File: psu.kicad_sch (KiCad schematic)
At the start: 21 parts, among them J17 Barrel_Jack_Switch, J18 USB_C_Receptacle_USB2.0_16P

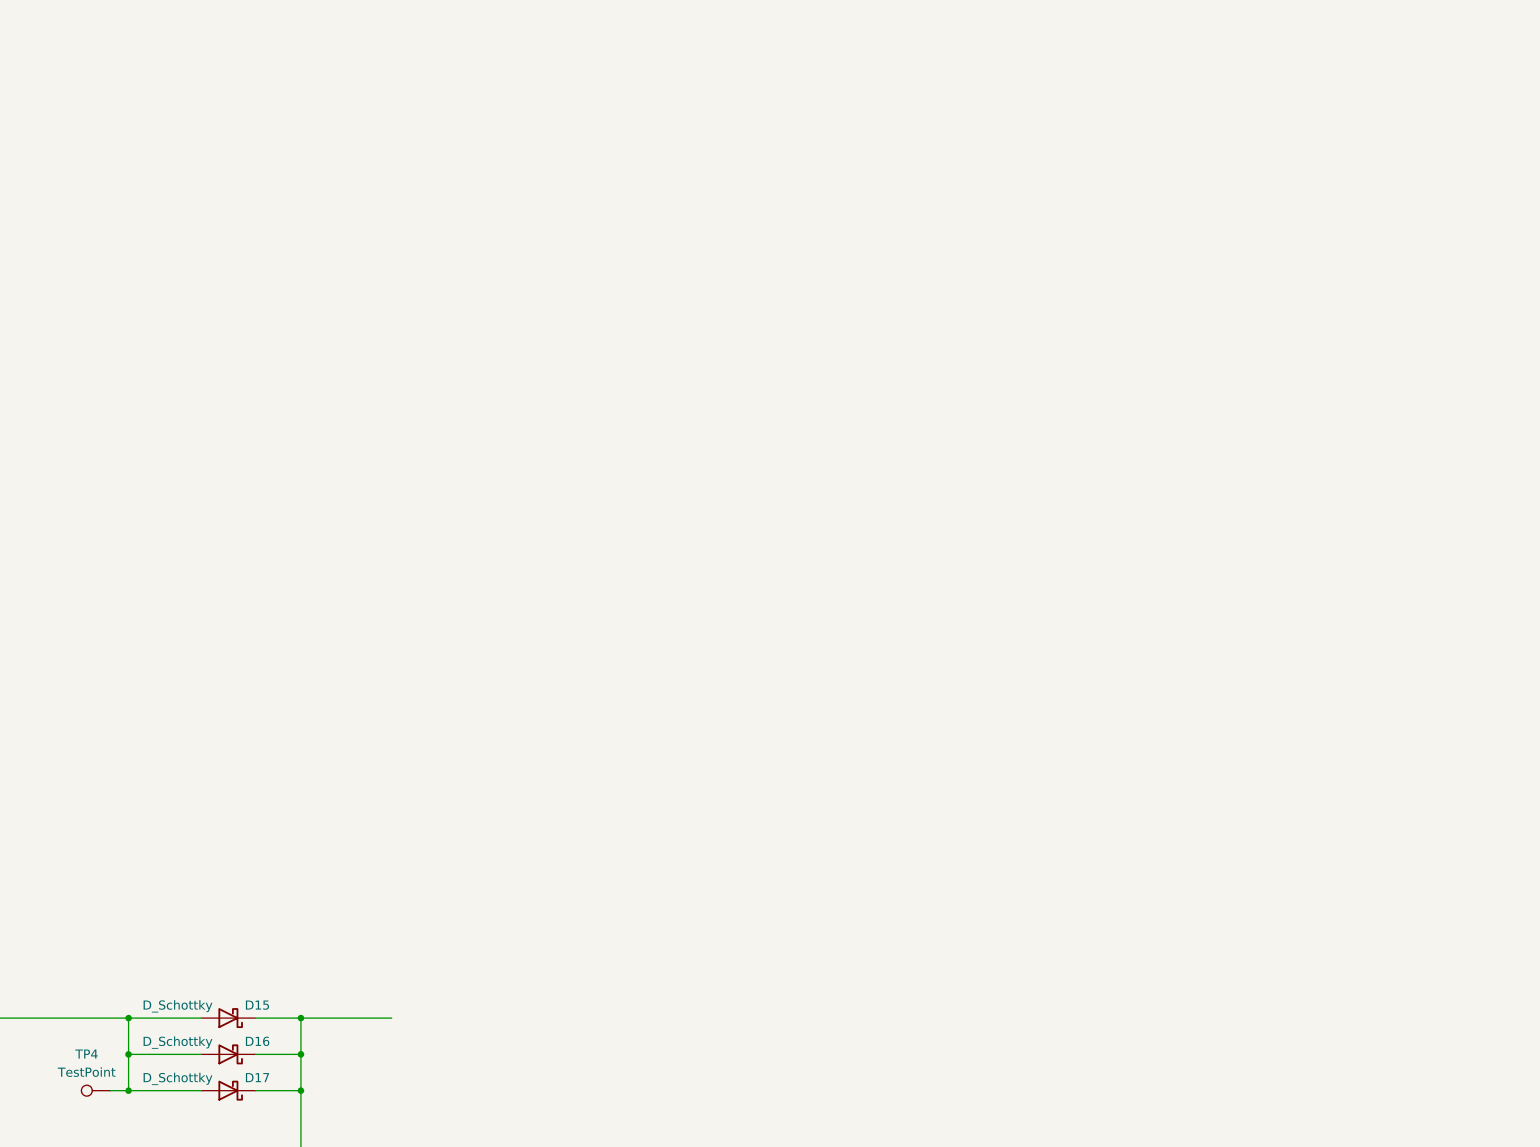
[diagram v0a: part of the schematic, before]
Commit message: feat(psu): Added PCIe power
- Do not populate, but there for future possible use.
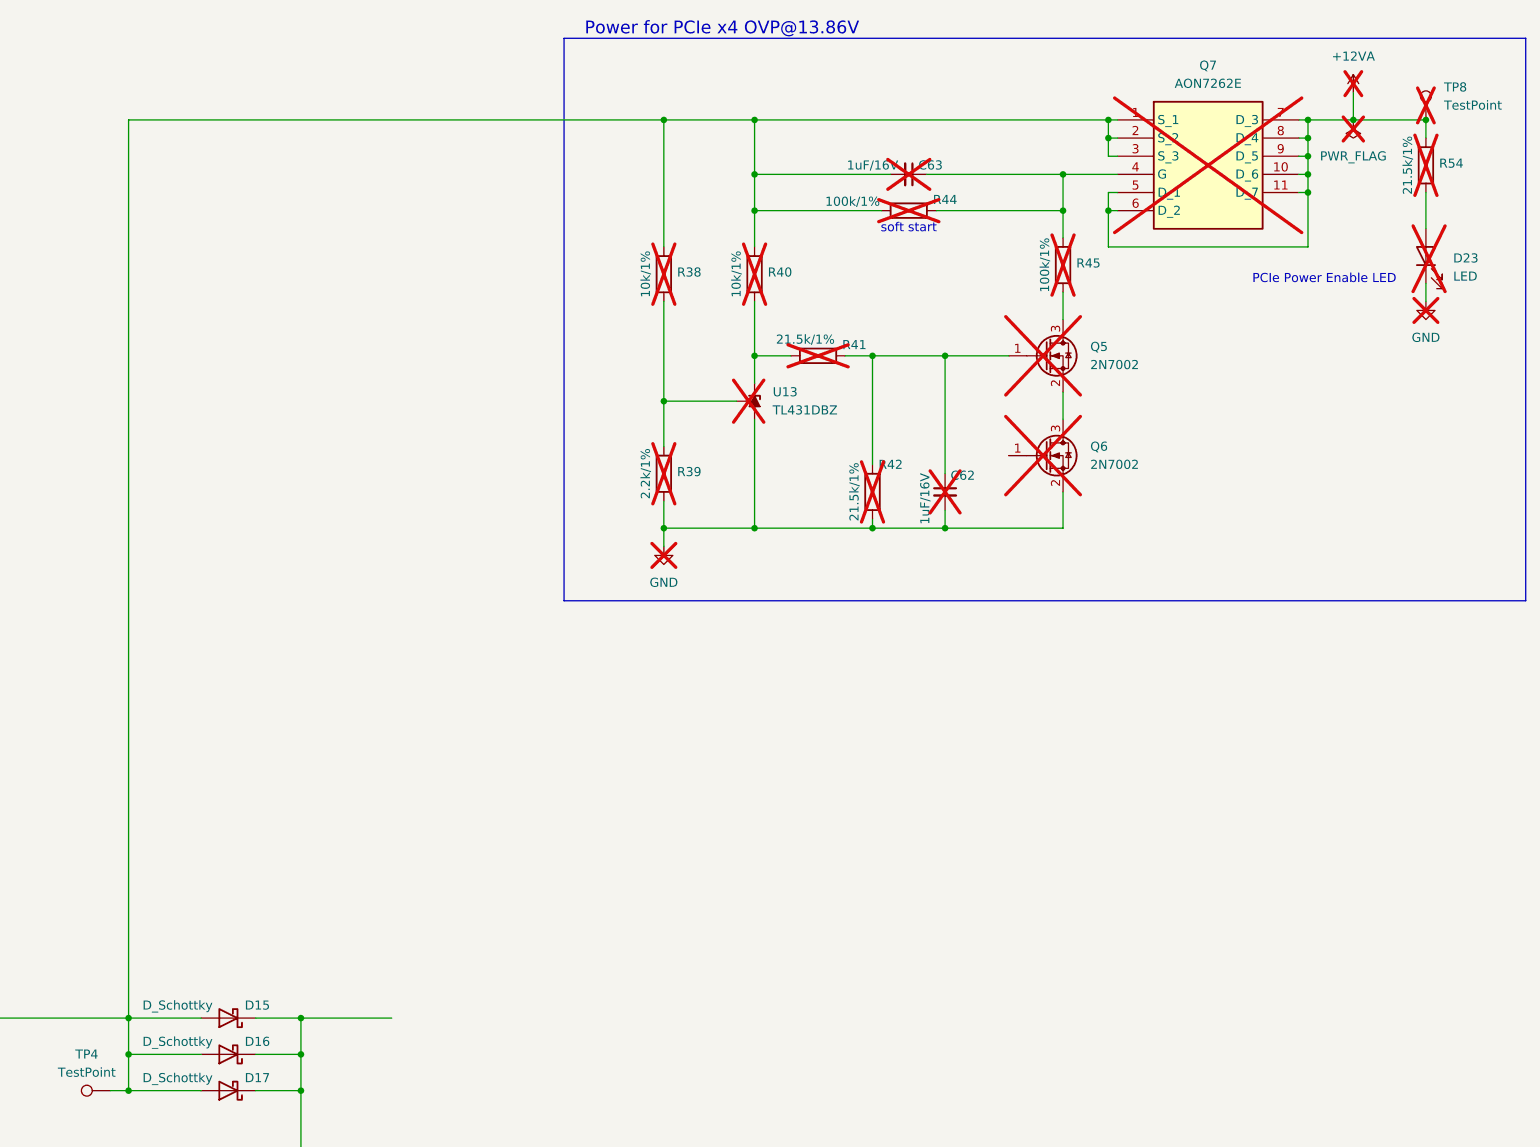
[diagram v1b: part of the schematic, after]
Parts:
- added C62, C63: 1uF/16V, A_HDJ_Library:C_0402_1005Metric, symbol Device:C_Small
- added D23: LED, A_HDJ_Library:LED_0603_1608Metric, symbol Device:LED
- added Q5, Q6: 2N7002, A_HDJ_Library:SOT-23, symbol Transistor_FET:2N7002
- added Q7: AON7262E, A_HDJ_Library:MOSFET_PDFN8_3.3x3.3, symbol A_HDJ_Library:AON7262E
- added R38, R40: 10k/1%, A_HDJ_Library:R_0402_1005Metric, symbol Device:R
- added R39: 2.2k/1%, A_HDJ_Library:R_0402_1005Metric, symbol Device:R
- added R41, R42, R54: 21.5k/1%, A_HDJ_Library:R_0402_1005Metric, symbol Device:R
- added R44, R45: 100k/1%, A_HDJ_Library:R_0402_1005Metric, symbol Device:R
- added TP8: TestPoint, symbol Connector:TestPoint
- added U13: TL431DBZ, A_HDJ_Library:SOT-23, symbol Reference_Voltage:TL431DBZ
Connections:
- net GND: now also C62.2, D23.1 (K), Q6.2 (S), R39.1, R42.1, U13.3 (A)
- net at D15.2 (A), D16.2 (A), D17.2 (A)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: now also C63.2, Q7.1 (S_1), Q7.2 (S_2), Q7.3 (S_3), R38.2, R40.2, R44.1
- new net: R38.1, R39.2, U13.2 (REF)
- new net: R40.1, R41.1, U13.1 (K)
- new net: C62.1, Q5.1 (G), R41.2, R42.2
- new net: Q5.2 (S), Q6.3 (D)
- new net: D23.2 (A), R54.1
- new net: C63.1, Q7.4 (G), R44.2, R45.2
- new net: Q5.3 (D), R45.1
- new net +12VA: Q7.10 (D_6), Q7.11 (D_7), Q7.5 (D_1), Q7.6 (D_2), Q7.7 (D_3), Q7.8 (D_4), Q7.9 (D_5), R54.2, TP8.1
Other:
- note added: "PCIe Power Enable LED"
- note added: "Power for PCIe x4 OVP@13.86V"
- note added: "soft start"

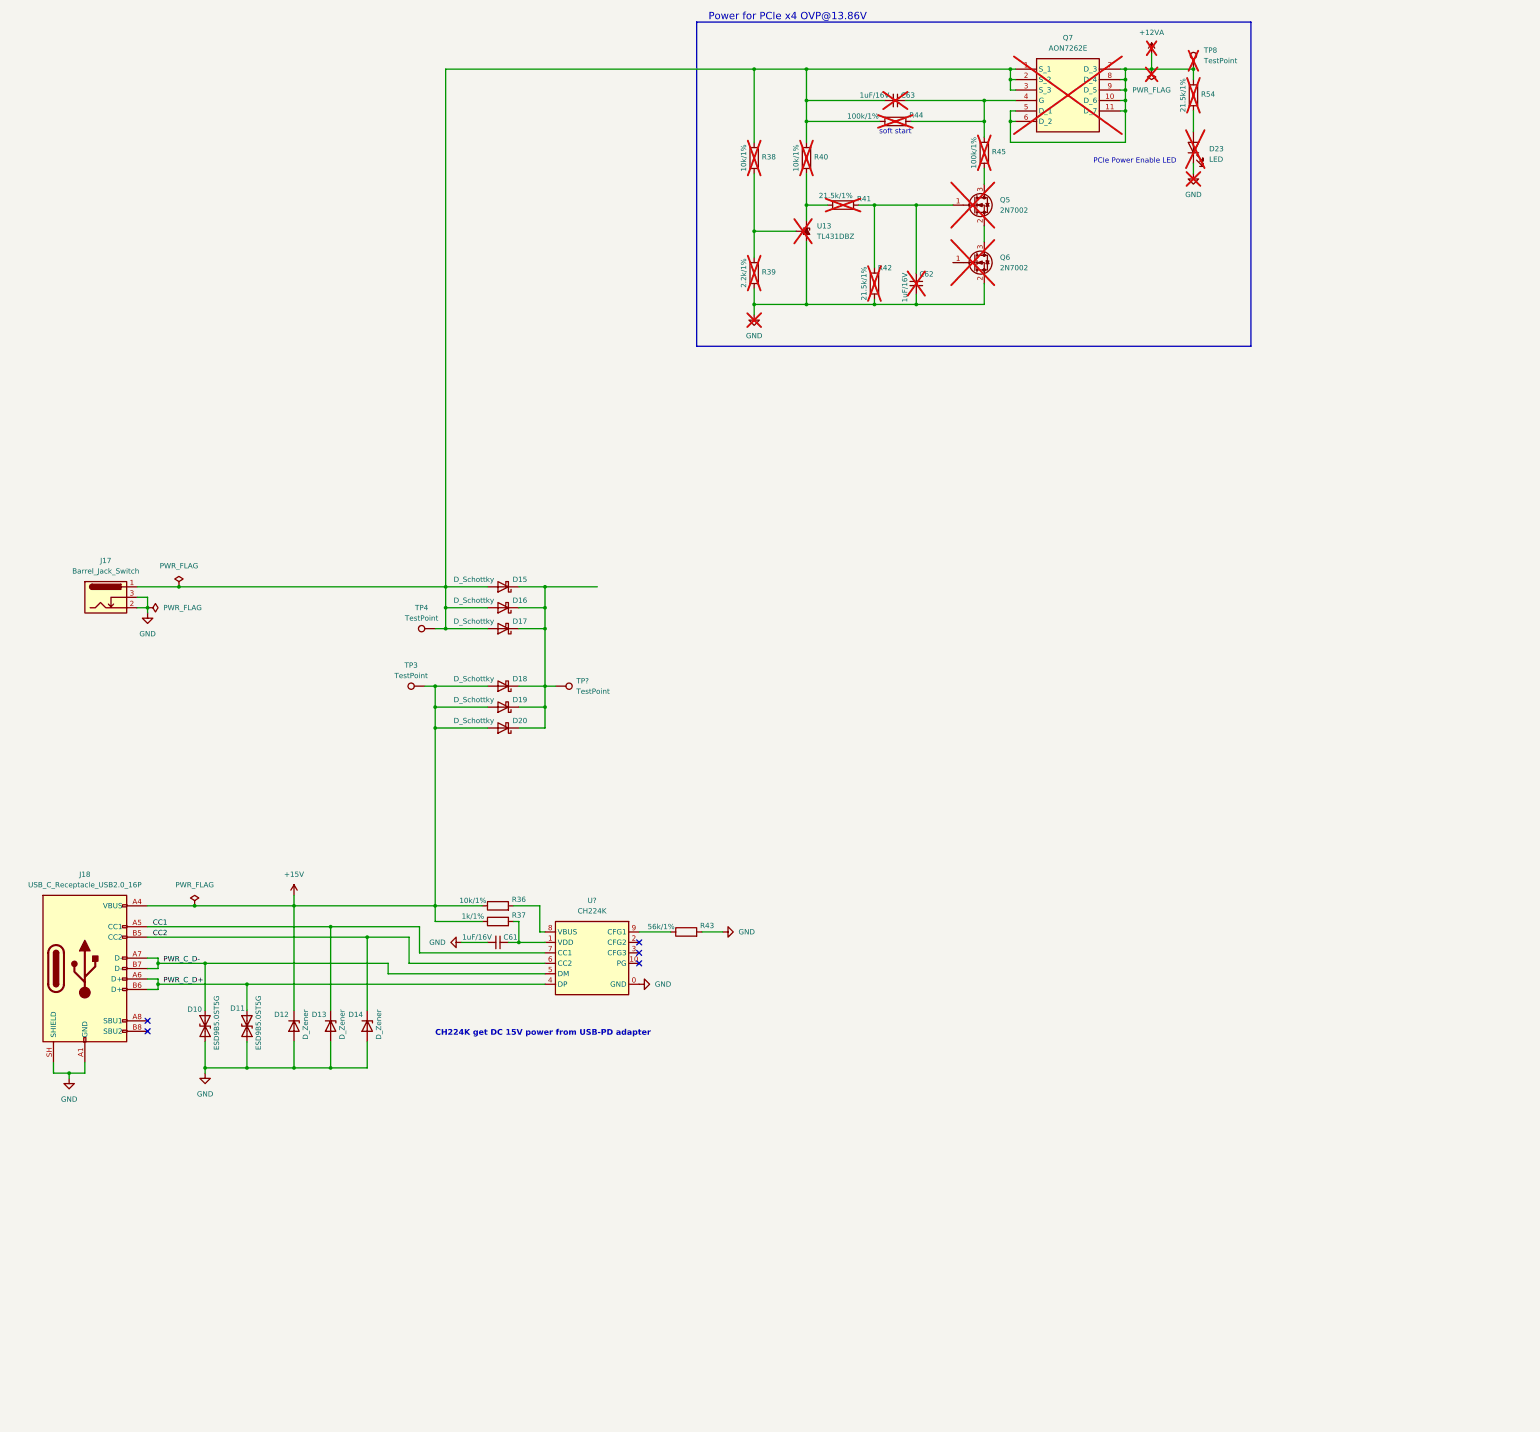
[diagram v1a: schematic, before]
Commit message: feat(psu): Added 5V and 3.3V outputs
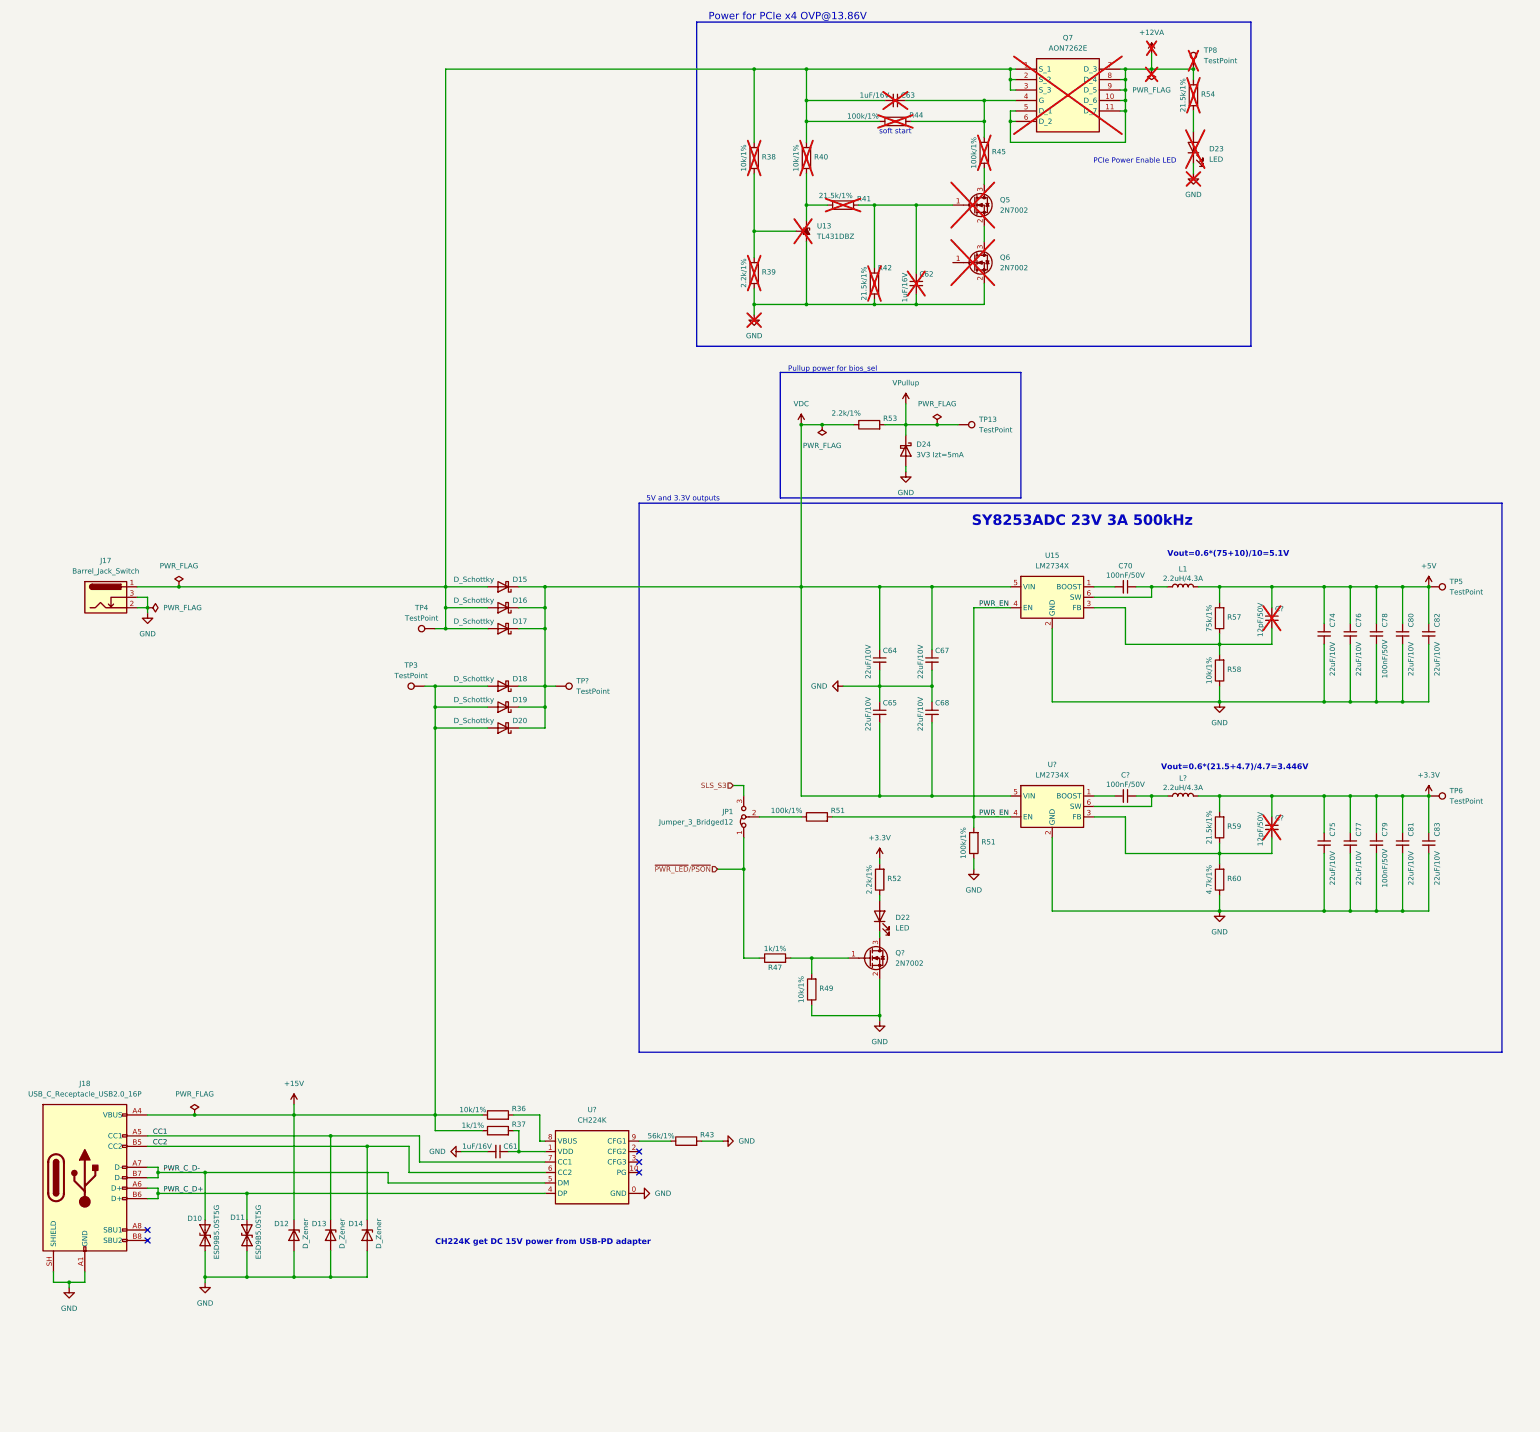
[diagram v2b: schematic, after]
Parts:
- added C64, C65, C67, C68, C74, C75, C76, C77, C80, C81, C82, C83: 22uF/10V, A_HDJ_Library:C_0603_1608Metric, symbol Device:C_Small
- added C70, C78, C79, C?: 100nF/50V, A_HDJ_Library:C_0603_1608Metric, symbol Device:C_Small
- added C? (x2): 12pF/50V, A_HDJ_Library:C_0402_1005Metric, symbol Device:C_Small
- added D22: LED, A_HDJ_Library:LED_0603_1608Metric, symbol Device:LED
- added D24: 3V3 Izt=5mA, A_HDJ_Library:D_SOD-323, symbol Device:D_Schottky
- added JP1: Jumper_3_Bridged12, symbol Jumper:Jumper_3_Bridged12
- added L1, L?: 2.2uH/4.3A, A_HDJ_Library:L_Sunlord_SWPA4020S, symbol Device:L
- added Q?: 2N7002, A_HDJ_Library:SOT-23, symbol Transistor_FET:2N7002
- added R47: 1k/1%, A_HDJ_Library:R_0402_1005Metric, symbol Device:R
- added R49, R58: 10k/1%, A_HDJ_Library:R_0402_1005Metric, symbol Device:R
- added R51 (x2): 100k/1%, A_HDJ_Library:R_0402_1005Metric, symbol Device:R
- added R52, R53: 2.2k/1%, A_HDJ_Library:R_0402_1005Metric, symbol Device:R
- added R57: 75k/1%, A_HDJ_Library:R_0402_1005Metric, symbol Device:R
- added R59: 21.5k/1%, A_HDJ_Library:R_0402_1005Metric, symbol Device:R
- added R60: 4.7k/1%, A_HDJ_Library:R_0402_1005Metric, symbol Device:R
- added TP13, TP5, TP6: TestPoint, symbol Connector:TestPoint
- added U15, U?: LM2734X, A_HDJ_Library:TSOT-23-6, symbol Regulator_Switching:LM2734X
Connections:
- net GND: now also C64.2, C65.1, C67.2, C68.1, C74.2, C75.2, C76.2, C77.2, C78.2, C79.2, C80.2, C81.2, C82.2, C83.2, D24.2 (A), Q?.2 (S), R49.1, R51.1, R58.1, R60.1, U15.2 (GND), U?.2 (GND)
- net VDC: now reaches D15.1 (K), D16.1 (K), D17.1 (K), D18.1 (K), D19.1 (K), D20.1 (K), TP?.1
- net VDC: now also C64.1, C65.2, C67.1, C68.2, R53.1, U15.5 (VIN), U?.5 (VIN)
- new net: C?.1, L?.1, U?.6 (SW)
- new net: C?.2, U?.1 (BOOST)
- new net: C70.2, U15.1 (BOOST)
- new net: C?.2, R57.1, R58.2, U15.3 (FB)
- new net: C70.1, L1.1, U15.6 (SW)
- new net: JP1.2 (C), R51.1
- new net: Q?.1 (G), R47.2, R49.2
- new net: D22.1 (K), Q?.3 (D)
- new net: C?.2, R59.1, R60.2, U?.3 (FB)
- new net: D22.2 (A), R52.1
- new net +3.3V: C75.1, C77.1, C79.1, C81.1, C83.1, C?.1, L?.2, R52.2, R59.2, TP6.1
- new net +5V: C74.1, C76.1, C78.1, C80.1, C82.1, C?.1, L1.2, R57.2, TP5.1
- new net PWR_EN: R51.2, R51.2, U15.4 (EN), U?.4 (EN)
- new net SLS_S3: JP1.3 (B)
- new net VPullup: D24.1 (K), R53.2, TP13.1
- new net ~{PWR_LED}/~{PSON}: JP1.1 (A), R47.1
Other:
- note added: "5V and 3.3V outputs"
- note added: "Pullup power for bios_sel"
- note added: "SY8253ADC 23V 3A 500kHz"
- note added: "Vout=0.6*(21.5+4.7)/4.7=3.446V"
- note added: "Vout=0.6*(75+10)/10=5.1V"
- moved on the sheet: C61, D10, D11, D12, D13, D14, J18, R36, R37, R43, U?
